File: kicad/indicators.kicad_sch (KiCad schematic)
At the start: 28 parts, among them U14 74LS244

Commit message: New decoding and GALs
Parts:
- added D1: DUARTB_TX, symbol Device:LED
- added D1: DUARTB_RX, symbol Device:LED
- added R20 (x2): R330, symbol Device:R
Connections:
- net GND: now also U14.1 (OEa), U14.19 (OEb), R20.1, R20.1
- net at D3.1 (K): now also U14.16 (O1a); no longer R19.2
- net at D3.2 (A): now also R19.2; no longer U14.16 (O1a)
- net at D2.1 (K): now also U14.12 (O3a); no longer R18.2
- net at D2.2 (A): now also R18.2; no longer U14.12 (O3a)
- net TXDA: now reaches U14.11 (I0b)
- net RXDB: now reaches U14.13 (I1b)
- net TXDB: now reaches U14.15 (I2b)
- net FC0: now reaches U14.2 (I0a)
- net FC1: now reaches U14.4 (I1a)
- net at U14.5 (O2b): now also D1.2 (A)
- net FC2: now reaches U14.6 (I2a)
- net at U14.7 (O1b): now also D1.2 (A)
- net RXDA: now reaches U14.8 (I3a)
- net at D2.1 (K): now also U14.18 (O0a); no longer R18.2
- net at D2.2 (A): now also R18.2; no longer U14.18 (O0a)
- net at D1.1 (K): now also U14.14 (O2a); no longer R20.2
- net at D1.2 (A): now also R20.2; no longer U14.14 (O2a)
- net at D1.1 (K): now also U14.7 (O1b); no longer R20.2
- net at D1.2 (A): now also R20.2; no longer U14.7 (O1b)
- net ~{IRQ5}: now reaches U14.11 (I0b)
- net ~{IRQ6}: now reaches U14.13 (I1b)
- net ~{IRQ7}: now reaches U14.15 (I2b)
- net ~{IRQ1}: now reaches U14.2 (I0a)
- net ~{IRQ2}: now reaches U14.4 (I1a)
- net at U14.5 (O2b): now also D1.1 (K); no longer D1.2 (A)
- net ~{IRQ3}: now reaches U14.6 (I2a)
- net ~{IRQ4}: now reaches U14.8 (I3a)
- net at U14.9 (O0b): now also D3.1 (K); no longer D3.2 (A)
- net at R20.2: now also D1.2 (A); no longer D1.1 (K)
- net at R19.2: now also D3.2 (A); no longer D3.1 (K)
- new net: D1.1 (K), R20.2 (x2)
- no-connect marks 0 -> 4
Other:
- moved on the sheet: D1, D2, D3

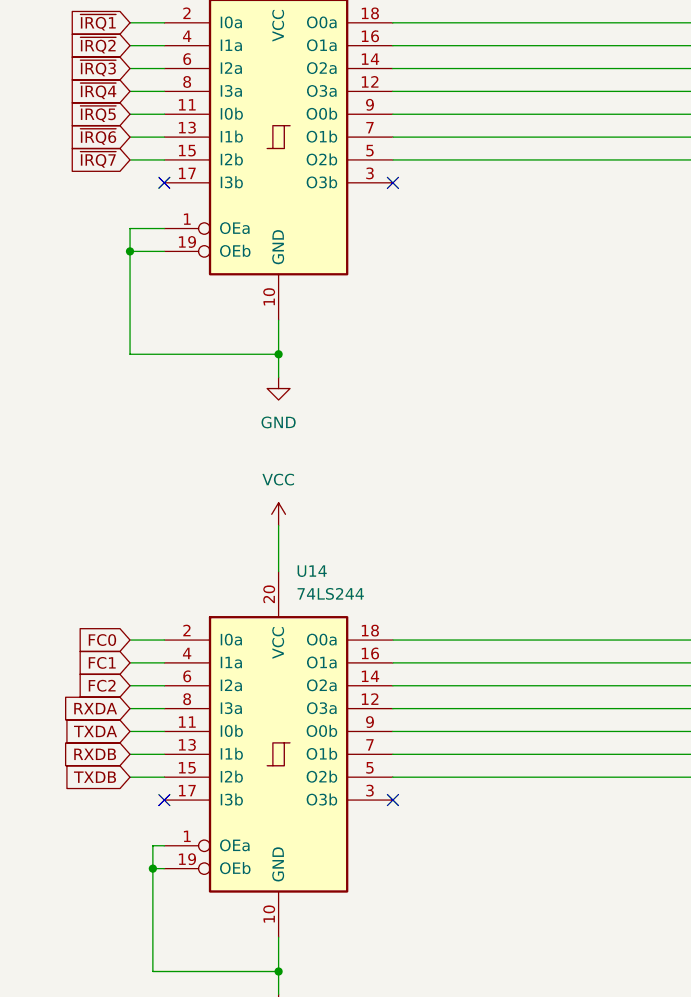
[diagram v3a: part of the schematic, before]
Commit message: added footprints
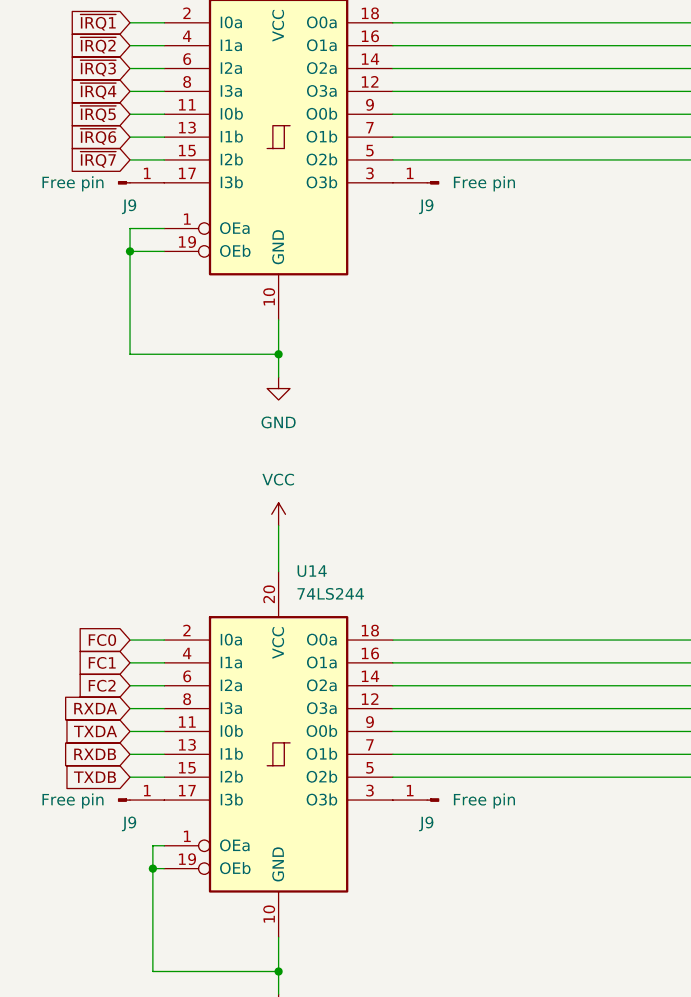
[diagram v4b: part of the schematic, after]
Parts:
- added J9 (x4): Free pin, Connector_PinSocket_2.54mm:PinSocket_1x01_P2.54mm_Vertical, symbol Connector:Conn_01x01_Pin
- D1, D2, D3: footprint (none) -> LED_THT:LED_D5.0mm
- U14: footprint (none) -> Package_DIP:DIP-20_W7.62mm_Socket
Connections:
- net at U14.17 (I3b): now also J9.1 (Pin_1) (x2)
- net at U14.3 (O3b): now also J9.1 (Pin_1) (x2)
- no-connect marks 4 -> 0

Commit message: updated readme
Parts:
- R18, R19, R20: footprint (none) -> Resistor_THT:R_Axial_DIN0207_L6.3mm_D2.5mm_P10.16mm_Horizontal
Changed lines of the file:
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@@
       (effects (font (size 1.27 1.27)))
     )
-    (property "Footprint" "" (at 219.71 129.032 90)
+    (property "Footprint" "Resistor_THT:R_Axial_DIN0207_L6.3mm_D2.5mm_P10.16mm_Horizontal" (at 219.71 129.032 90)
       (effects (font (size 1.27 1.27)) hide)
     )
@@
         )
         (path "/e63e39d7-6ac0-4ffd-8aa3-1841a4541b55/1dea36bd-d6d9-4a08-972d-1edadec46a75"
-          (reference "#PWR055") (unit 1)
+          (reference "#PWR054") (unit 1)
         )
       )
@@
         )
         (path "/e63e39d7-6ac0-4ffd-8aa3-1841a4541b55/1dea36bd-d6d9-4a08-972d-1edadec46a75"
-          (reference "J19") (unit 1)
+          (reference "J17") (unit 1)
         )
       )
@@
         )
         (path "/e63e39d7-6ac0-4ffd-8aa3-1841a4541b55/1dea36bd-d6d9-4a08-972d-1edadec46a75"
-          (reference "#PWR056") (unit 1)
+          (reference "#PWR055") (unit 1)
         )
       )
@@
         )
         (path "/e63e39d7-6ac0-4ffd-8aa3-1841a4541b55/1dea36bd-d6d9-4a08-972d-1edadec46a75"
-          (reference "#PWR060") (unit 1)
+          (reference "#PWR059") (unit 1)
         )
       )
@@
         )
         (path "/e63e39d7-6ac0-4ffd-8aa3-1841a4541b55/1dea36bd-d6d9-4a08-972d-1edadec46a75"
-          (reference "#PWR059") (unit 1)
+          (reference "#PWR058") (unit 1)
         )
       )
@@
       (effects (font (size 1.27 1.27)))
     )
-    (property "Footprint" "" (at 219.71 120.142 90)
+    (property "Footprint" "Resistor_THT:R_Axial_DIN0207_L6.3mm_D2.5mm_P10.16mm_Horizontal" (at 219.71 120.142 90)
       (effects (font (size 1.27 1.27)) hide)
     )
@@
       (effects (font (size 1.27 1.27)))
     )
-    (property "Footprint" "" (at 218.44 33.782 90)
+    (property "Footprint" "Resistor_THT:R_Axial_DIN0207_L6.3mm_D2.5mm_P10.16mm_Horizontal" (at 218.44 33.782 90)
       (effects (font (size 1.27 1.27)) hide)
     )
@@
         )
         (path "/e63e39d7-6ac0-4ffd-8aa3-1841a4541b55/1dea36bd-d6d9-4a08-972d-1edadec46a75"
-          (reference "C23") (unit 1)
+          (reference "C24") (unit 1)
         )
       )
@@
         )
         (path "/e63e39d7-6ac0-4ffd-8aa3-1841a4541b55/1dea36bd-d6d9-4a08-972d-1edadec46a75"
-          (reference "#PWR058") (unit 1)
+          (reference "#PWR057") (unit 1)
         )
       )
@@
       (effects (font (size 1.27 1.27)))
     )
-    (property "Footprint" "" (at 219.71 137.922 90)
+    (property "Footprint" "Resistor_THT:R_Axial_DIN0207_L6.3mm_D2.5mm_P10.16mm_Horizontal" (at 219.71 137.922 90)
       (effects (font (size 1.27 1.27)) hide)
     )
@@
         )
         (path "/e63e39d7-6ac0-4ffd-8aa3-1841a4541b55/1dea36bd-d6d9-4a08-972d-1edadec46a75"
-          (reference "J17") (unit 1)
+          (reference "J16") (unit 1)
         )
       )
@@
       (effects (font (size 1.27 1.27)))
     )
-    (property "Footprint" "" (at 219.71 146.812 90)
+    (property "Footprint" "Resistor_THT:R_Axial_DIN0207_L6.3mm_D2.5mm_P10.16mm_Horizontal" (at 219.71 146.812 90)
       (effects (font (size 1.27 1.27)) hide)
     )
@@
       (effects (font (size 1.27 1.27)))
     )
-    (property "Footprint" "" (at 218.44 78.232 90)
+    (property "Footprint" "Resistor_THT:R_Axial_DIN0207_L6.3mm_D2.5mm_P10.16mm_Horizontal" (at 218.44 78.232 90)
       (effects (font (size 1.27 1.27)) hide)
     )
@@
       (effects (font (size 1.27 1.27)))
     )
-    (property "Footprint" "" (at 219.71 155.702 90)
+    (property "Footprint" "Resistor_THT:R_Axial_DIN0207_L6.3mm_D2.5mm_P10.16mm_Horizontal" (at 219.71 155.702 90)
       (effects (font (size 1.27 1.27)) hide)
     )
@@
         )
         (path "/e63e39d7-6ac0-4ffd-8aa3-1841a4541b55/1dea36bd-d6d9-4a08-972d-1edadec46a75"
-          (reference "#PWR062") (unit 1)
+          (reference "#PWR061") (unit 1)
         )
       )
@@
       (effects (font (size 1.27 1.27)))
     )
-    (property "Footprint" "" (at 218.44 60.452 90)
+    (property "Footprint" "Resistor_THT:R_Axial_DIN0207_L6.3mm_D2.5mm_P10.16mm_Horizontal" (at 218.44 60.452 90)
       (effects (font (size 1.27 1.27)) hide)
     )
@@
         )
         (path "/e63e39d7-6ac0-4ffd-8aa3-1841a4541b55/1dea36bd-d6d9-4a08-972d-1edadec46a75"
-          (reference "#PWR057") (unit 1)
+          (reference "#PWR056") (unit 1)
         )
       )
@@
       (effects (font (size 1.27 1.27)))
     )
-    (property "Footprint" "" (at 218.44 69.342 90)
+    (property "Footprint" "Resistor_THT:R_Axial_DIN0207_L6.3mm_D2.5mm_P10.16mm_Horizontal" (at 218.44 69.342 90)
       (effects (font (size 1.27 1.27)) hide)
     )
@@
       (effects (font (size 1.27 1.27)))
     )
-    (property "Footprint" "" (at 218.44 87.122 90)
+    (property "Footprint" "Resistor_THT:R_Axial_DIN0207_L6.3mm_D2.5mm_P10.16mm_Horizontal" (at 218.44 87.122 90)
       (effects (font (size 1.27 1.27)) hide)
     )
@@
       (effects (font (size 1.27 1.27)))
     )
-    (property "Footprint" "" (at 219.71 111.252 90)
+    (property "Footprint" "Resistor_THT:R_Axial_DIN0207_L6.3mm_D2.5mm_P10.16mm_Horizontal" (at 219.71 111.252 90)
       (effects (font (size 1.27 1.27)) hide)
     )
@@
       (effects (font (size 1.27 1.27)))
     )
-    (property "Footprint" "" (at 218.44 42.672 90)
+    (property "Footprint" "Resistor_THT:R_Axial_DIN0207_L6.3mm_D2.5mm_P10.16mm_Horizontal" (at 218.44 42.672 90)
       (effects (font (size 1.27 1.27)) hide)
     )
@@
       (effects (font (size 1.27 1.27)))
     )
-    (property "Footprint" "" (at 219.71 102.362 90)
+    (property "Footprint" "Resistor_THT:R_Axial_DIN0207_L6.3mm_D2.5mm_P10.16mm_Horizontal" (at 219.71 102.362 90)
       (effects (font (size 1.27 1.27)) hide)
     )
@@
         )
         (path "/e63e39d7-6ac0-4ffd-8aa3-1841a4541b55/1dea36bd-d6d9-4a08-972d-1edadec46a75"
-          (reference "J20") (unit 1)
+          (reference "J19") (unit 1)
         )
       )
@@
         )
         (path "/e63e39d7-6ac0-4ffd-8aa3-1841a4541b55/1dea36bd-d6d9-4a08-972d-1edadec46a75"
-          (reference "#PWR061") (unit 1)
+          (reference "#PWR060") (unit 1)
         )
       )
@@
       (effects (font (size 1.27 1.27)))
     )
-    (property "Footprint" "" (at 218.44 51.562 90)
+    (property "Footprint" "Resistor_THT:R_Axial_DIN0207_L6.3mm_D2.5mm_P10.16mm_Horizontal" (at 218.44 51.562 90)
       (effects (font (size 1.27 1.27)) hide)
     )
@@
         )
         (path "/e63e39d7-6ac0-4ffd-8aa3-1841a4541b55/1dea36bd-d6d9-4a08-972d-1edadec46a75"
-          (reference "C22") (unit 1)
-        )
-      )
+          (reference "C23") (unit 1)
+        )
+      )
